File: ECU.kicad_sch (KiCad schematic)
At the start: 96 parts, among them J1 Solenoid 0, J10 Thermocouple 3, J13 External SPI, J14 External UART, J15 External I2C, J16 Pressure Transducer 0, J17 Pressure Transducer 1, J18 Pressure Transducer 2, J19 Pressure Transducer 3, J2 Solenoid 1, J20 Pressure Transducer 4, J21 Pressure Transducer 5, J3 Solenoid 2, J4 Solenoid 3, J5 Solenoid 4, J6 Solenoid 5, J7 Thermocouple 0, J8 Thermocouple 1, J9 Thermocouple 2, U1 Teensy4.1, U10 MAX31855, U11 MAX31855, U12 OPA357, U13 OPA357, U14 OPA357, U15 OPA357, U16 OPA357, U17 OPA357, U2 OPA357, U3 OPA357, U4 OPA357, U5 OPA357, U6 OPA357, U7 OPA357, U8 MAX31855, U9 MAX31855

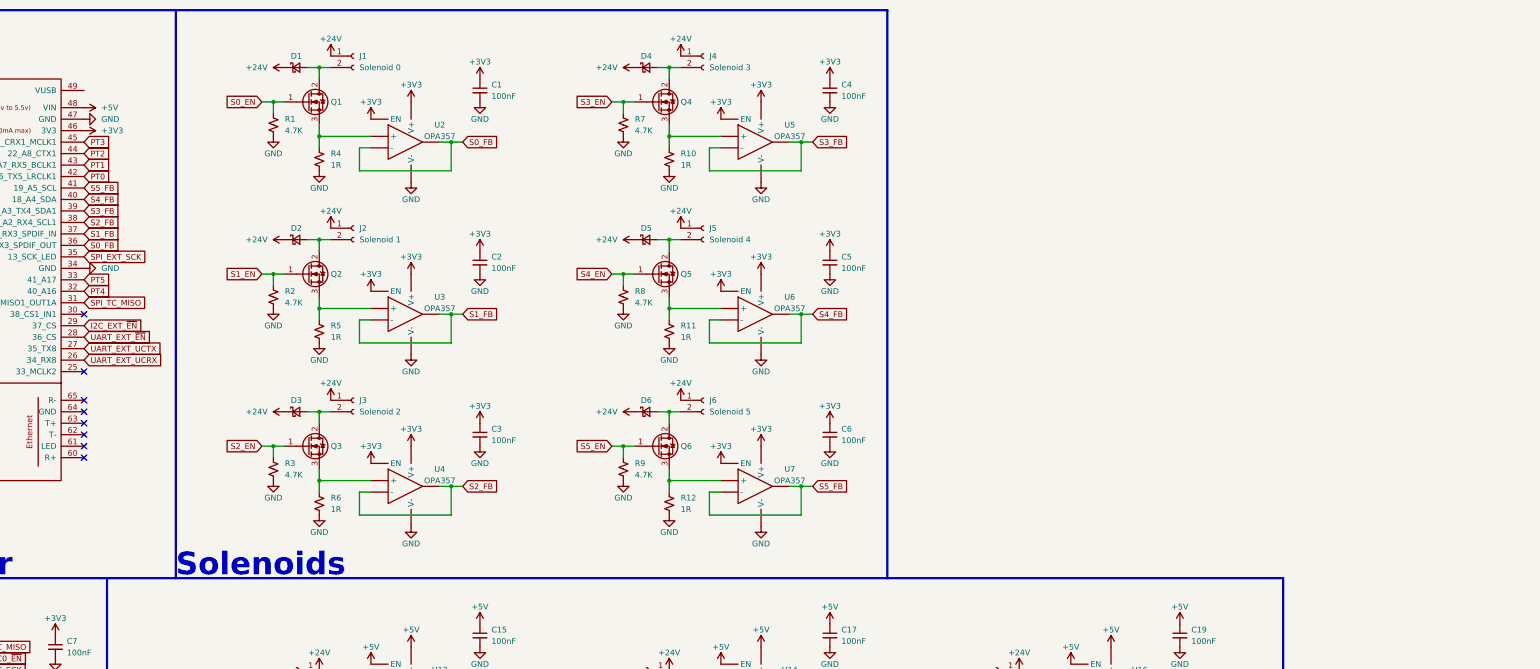
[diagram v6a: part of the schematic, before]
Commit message: Add power supply, indicators, & test points
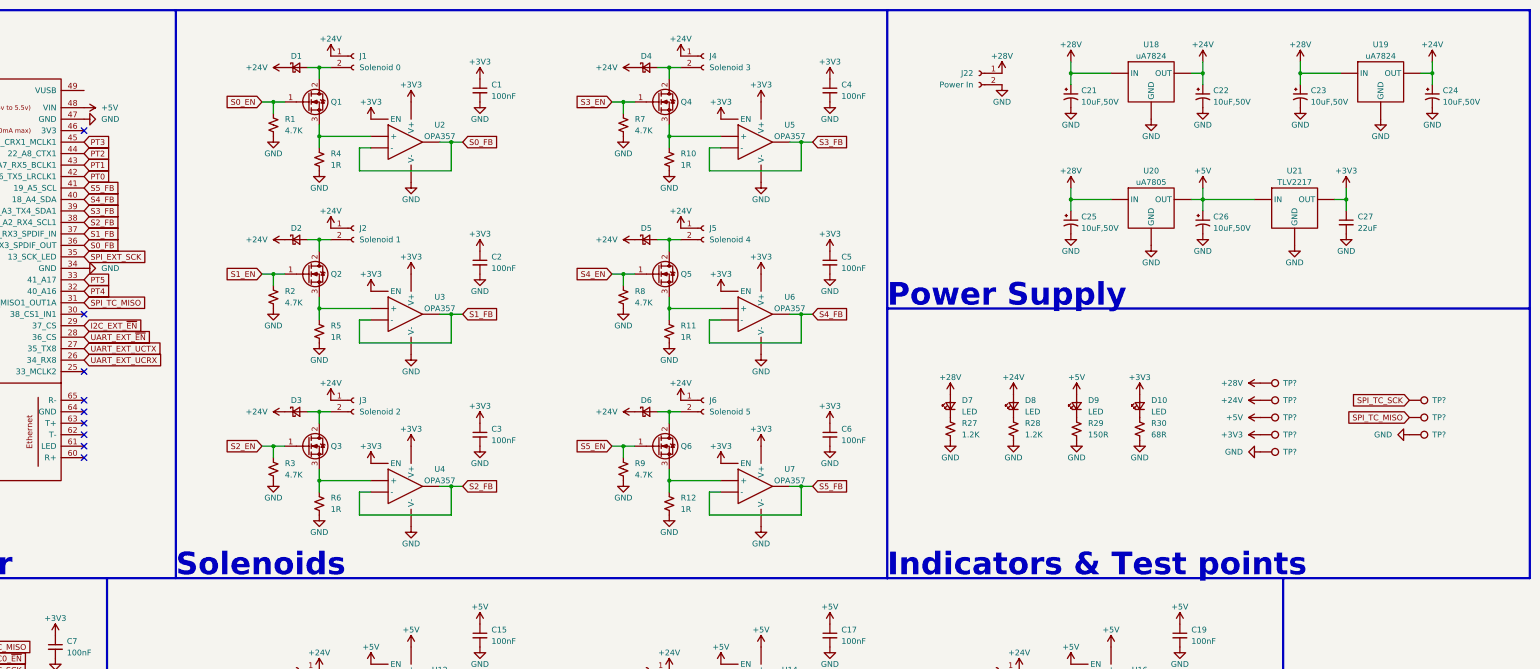
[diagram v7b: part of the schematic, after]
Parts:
- added C21, C22, C23, C24, C25, C26: 10uF,50V, Capacitor_SMD:CP_Elec_5x5.9, symbol Device:C_Polarized_Small_US
- added C27: 22uF, Capacitor_SMD:C_0805_2012Metric, symbol Device:C_Small
- added D10, D7, D8, D9: LED, Diode_SMD:D_0603_1608Metric, symbol Device:LED_Small
- added J22: Power In, TerminalBlock:TerminalBlock_bornier-2_P5.08mm, symbol Connector:Conn_01x02_Female
- added R27, R28: 1.2K, Resistor_SMD:R_0603_1608Metric, symbol Device:R_Small_US
- added R29: 150R, Resistor_SMD:R_0603_1608Metric, symbol Device:R_Small_US
- added R30: 68R, Resistor_SMD:R_0603_1608Metric, symbol Device:R_Small_US
- added TP? (x8): ~, symbol Connector:TestPoint
- added U18, U19: uA7824, Package_TO_SOT_THT:TO-220-3_Vertical, symbol ECU:uA78xx
- added U20: uA7805, Package_TO_SOT_THT:TO-220-3_Vertical, symbol ECU:uA78xx
- added U21: TLV2217, Package_TO_SOT_THT:TO-220-3_Vertical, symbol ECU:TLV2217
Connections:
- net +24V: now also C22.1, C24.1, D8.2 (A), TP?.1, U18.3 (OUT), U19.3 (OUT)
- net +3V3: now also C27.1, D10.2 (A), TP?.1, U21.3 (OUT); no longer U1.46 (3V3)
- net +5V: now also C26.1, D9.2 (A), TP?.1, U20.3 (OUT), U21.1 (IN)
- net GND: now also C21.2, C22.2, C23.2, C24.2, C25.2, C26.2, C27.2, J22.2 (Pin_2), R27.2, R28.2, R29.2, R30.2, TP?.1, TP?.1, U18.2 (GND), U19.2 (GND), U20.2 (GND), U21.2 (GND)
- net SPI_TC_MISO: now also TP?.1
- net SPI_TC_SCK: now also TP?.1
- new net: D8.1 (K), R28.1
- new net: D9.1 (K), R29.1
- new net: D7.1 (K), R27.1
- new net: D10.1 (K), R30.1
- new net +28V: C21.1, C23.1, C25.1, D7.2 (A), J22.1 (Pin_1), TP?.1, U18.1 (IN), U19.1 (IN), U20.1 (IN)
- no-connect marks 25 -> 26
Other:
- note added: "Indicators & Test points"
- note added: "Power Supply"

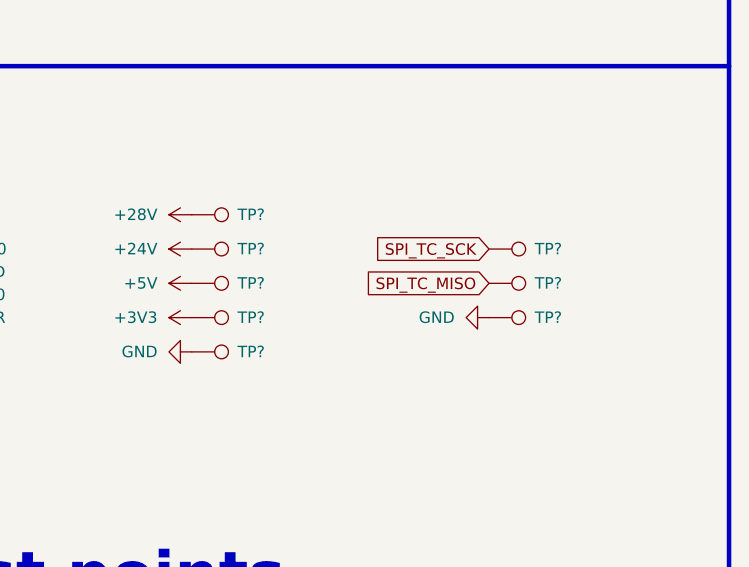
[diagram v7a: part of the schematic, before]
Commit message: Add PCB layout
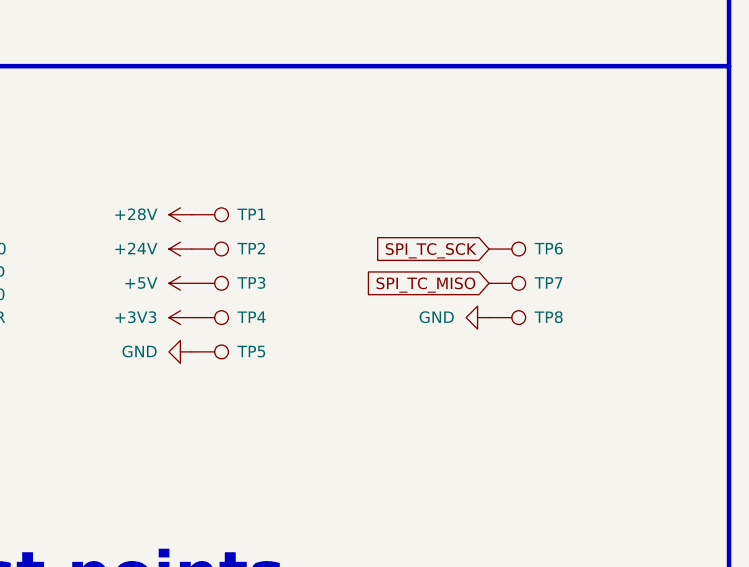
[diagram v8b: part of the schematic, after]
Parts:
- TP1, TP2, TP3, TP4, TP5, TP6, TP7, TP8: renamed from TP?; footprint (none) -> TestPoint:TestPoint_Pad_D4.0mm
